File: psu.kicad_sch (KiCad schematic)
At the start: 76 parts, among them J17 Barrel_Jack_Switch, J18 USB_C_Receptacle_USB2.0_16P, Q5 2N7002, Q6 2N7002, Q7 AON7262E, U13 TL431DBZ, U15 LM2734X

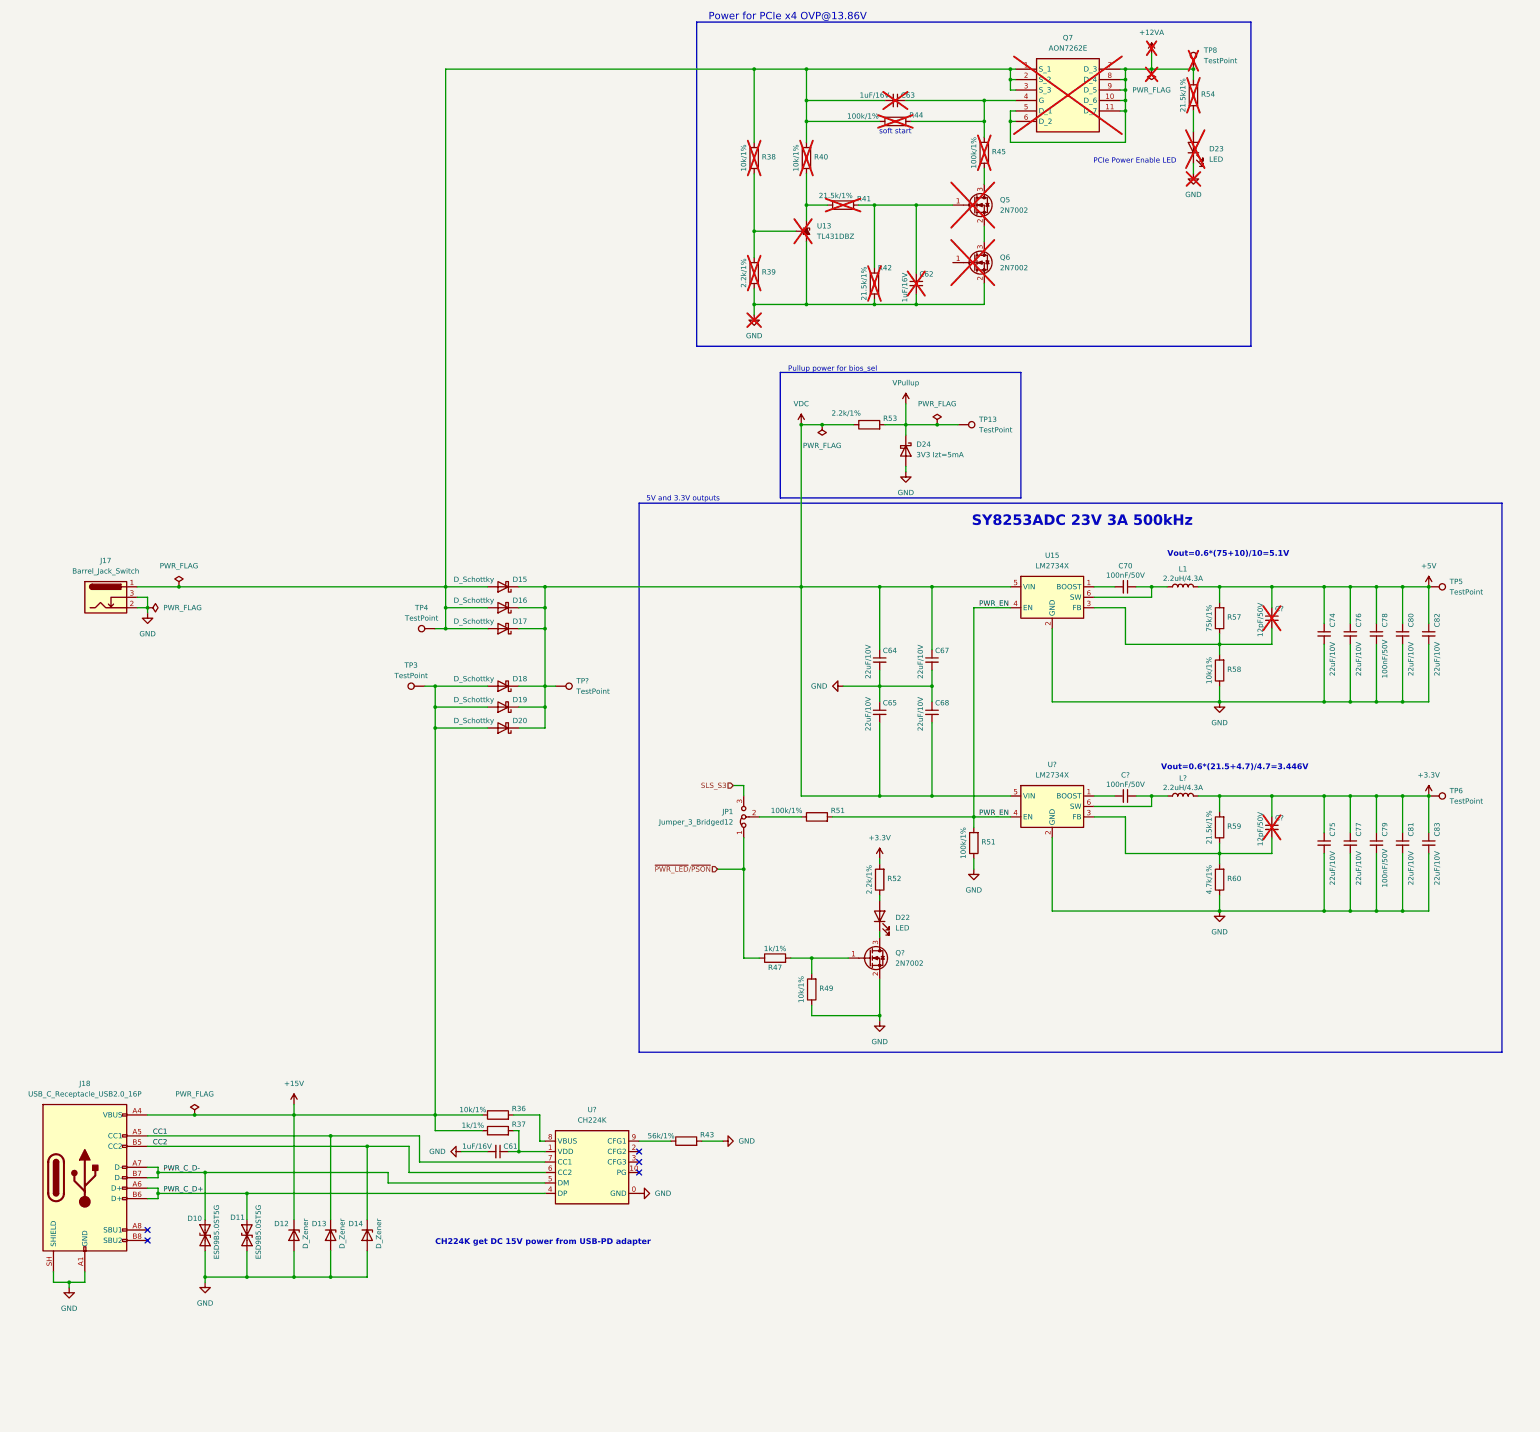
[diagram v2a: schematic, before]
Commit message: feat(psu): Added power and reset buttons
- Also added extra labels and documentation.
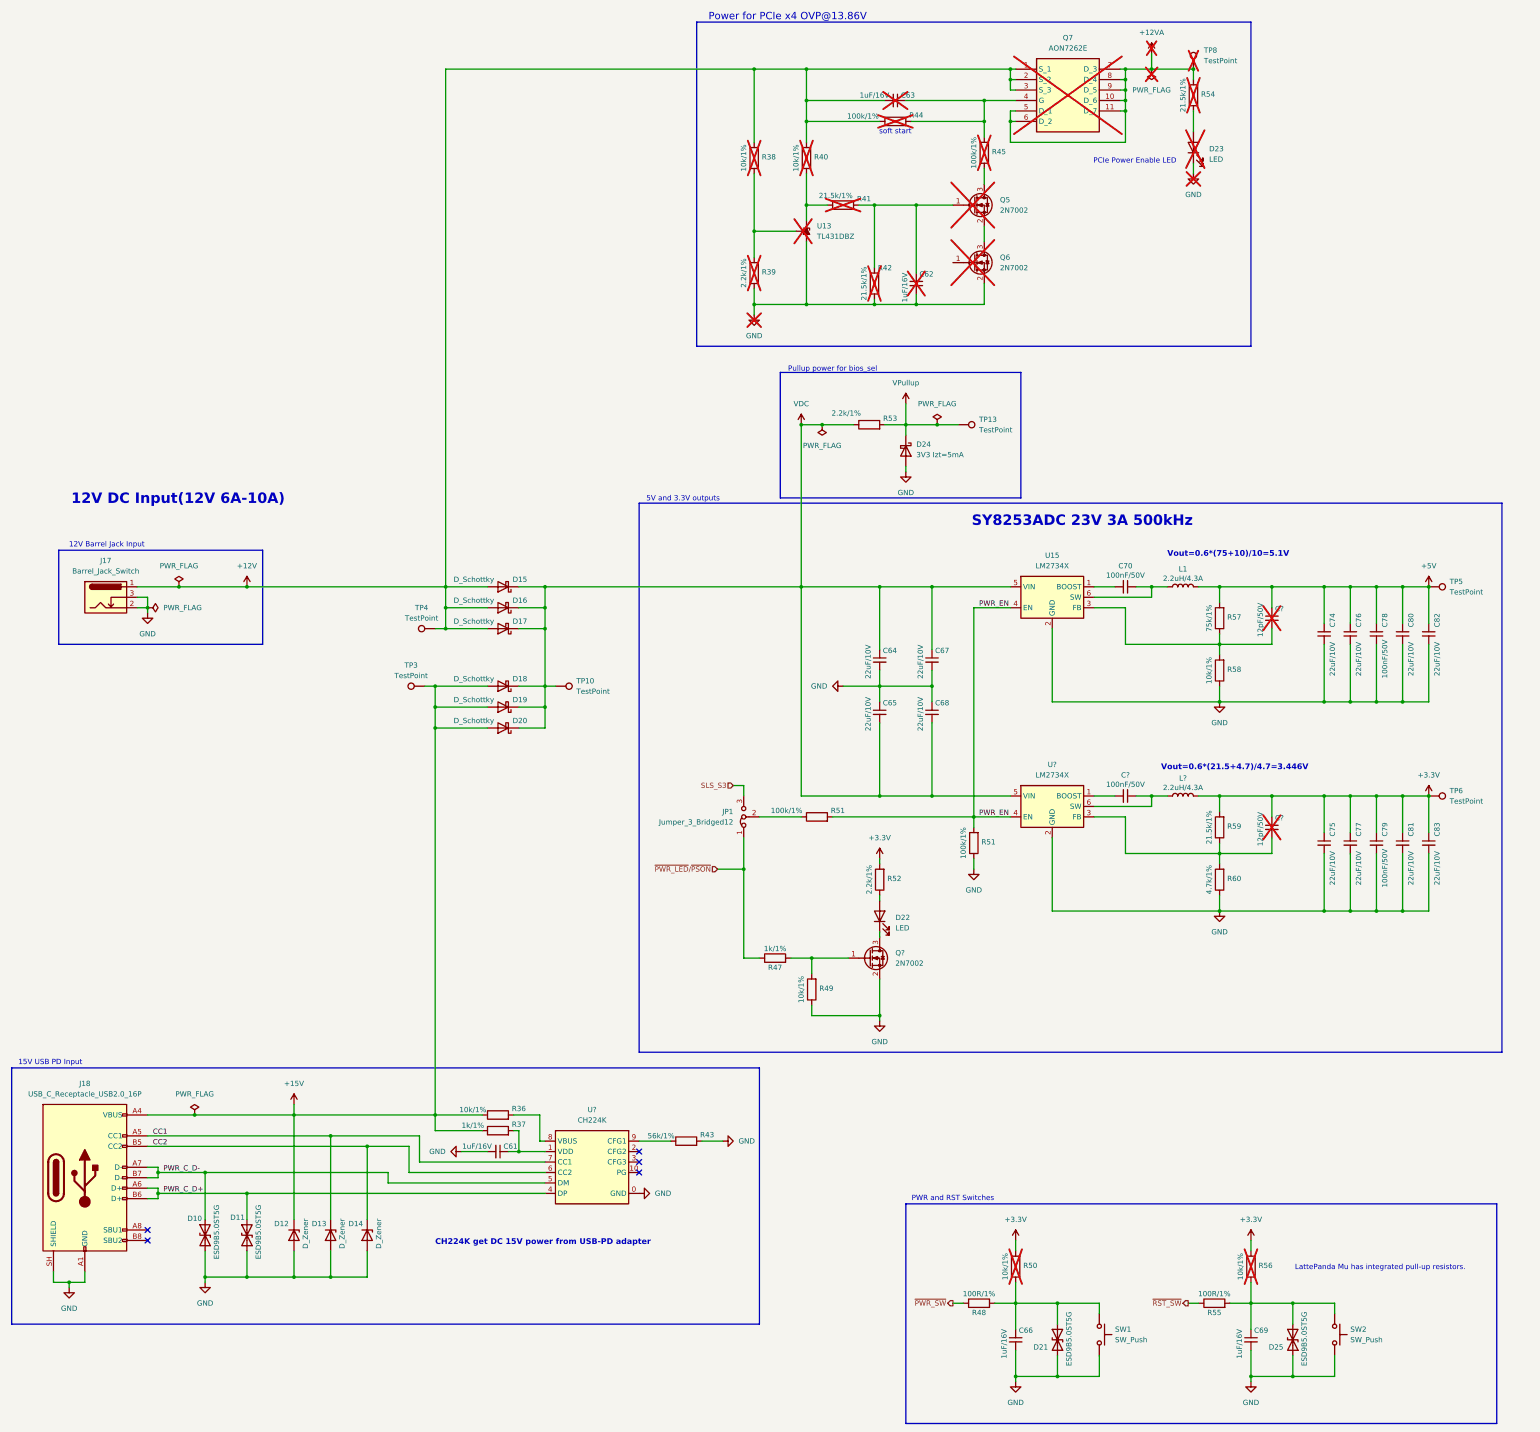
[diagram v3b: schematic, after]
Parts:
- added C66, C69: 1uF/16V, A_HDJ_Library:C_0402_1005Metric, symbol Device:C_Small
- added D21, D25: ESD9B5.0ST5G, Diode_SMD:D_0402_1005Metric, symbol Diode:ESD9B5.0ST5G
- added R48, R55: 100R/1%, A_HDJ_Library:R_0402_1005Metric, symbol Device:R
- added R50, R56: 10k/1%, A_HDJ_Library:R_0402_1005Metric, symbol Device:R
- added SW1, SW2: SW_Push, A_HDJ_Library:SW_Push_6x6x6, symbol Switch:SW_Push
- gave numbers to parts that had none: 1
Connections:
- net +3.3V: now also R50.2, R56.2
- net GND: now also C66.2, C69.2, D21.2 (A2), D25.2 (A2), SW1.2, SW2.2
- net +12V: now reaches C63.2, D15.2 (A), D16.2 (A), D17.2 (A), J17.1, Q7.1 (S_1), Q7.2 (S_2), Q7.3 (S_3), R38.2, R40.2, R44.1, TP4.1
- new net: C66.1, D21.1 (A1), R48.2, R50.1, SW1.1
- new net: C69.1, D25.1 (A1), R55.2, R56.1, SW2.1
- new net ~{PWR_SW}: R48.1
- new net ~{RST_SW}: R55.1
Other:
- note added: "12V Barrel Jack Input"
- note added: "12V DC Input(12V 6A-10A)"
- note added: "15V USB PD Input"
- note added: "LattePanda Mu has integrated pull-up resistors."
- note added: "PWR and RST Switches"

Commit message: feat: Ran ERC and fixed missing annotations and wiring errors
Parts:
- added TP9: TestPoint, symbol Connector:TestPoint
- gave numbers to parts that had none: 7
- renumbered R51 to R46
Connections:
- net PWR_EN: now also Q6.1 (G), TP9.1

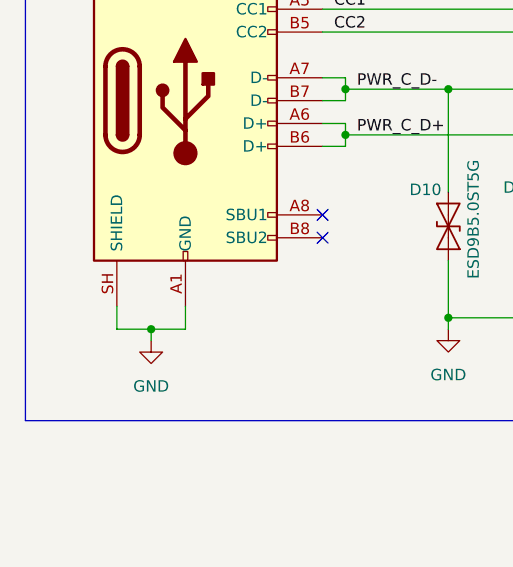
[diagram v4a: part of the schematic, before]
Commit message: fix: Set missing footprints and fixed missing pin-pad connections.
- J15, J16 missing MP1 and MP2 pins. Fixed in pin table within the symbol editor for each symbol.
- A ll USB receptacles J4, J5, J18 had mismatched pin numbers for the pcb symbol footprint. Renamed to match.
- Fixed various DNP components that were not excluded from the board.
- Fixed remaining missing footprints.
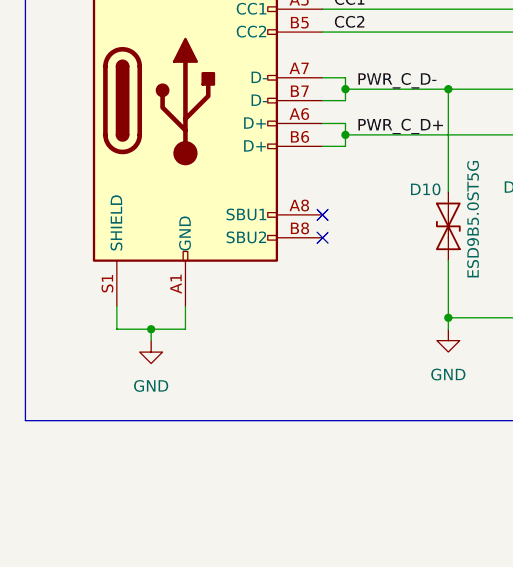
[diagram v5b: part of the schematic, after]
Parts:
- J18: footprint (none) -> A_HDJ_Library:USB_C_Receptacle_G-Switch_GT-USB-7010ASV
- JP1: footprint (none) -> A_HDJ_Library:PinHeader_1x03_P2.54mm_Vertical
- TP10, TP13, TP3, TP4, TP5, TP6, TP8, TP9: footprint (none) -> A_HDJ_Library:TestPoint_Pad_D1.5mm
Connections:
- net GND: now also J18.S1 (SHIELD); no longer J18.SH (SHIELD)

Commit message: fix: Fixed DNP parts populating on the board.
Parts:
- C62, C63, D23, Q5, Q6, Q7, R38, R39, R40, R41, R42, R44, R45, R50, R54, R56, TP8, TP9, U13: now left out of the parts list
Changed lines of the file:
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@@
 		(body_style 1)
 		(exclude_from_sim no)
-		(in_bom yes)
-		(on_board yes)
+		(in_bom no)
+		(on_board no)
 		(in_pos_files yes)
 		(dnp yes)
@@
 		(body_style 1)
 		(exclude_from_sim no)
-		(in_bom yes)
-		(on_board yes)
+		(in_bom no)
+		(on_board no)
 		(in_pos_files yes)
 		(dnp yes)
@@
 		(body_style 1)
 		(exclude_from_sim no)
-		(in_bom yes)
-		(on_board yes)
+		(in_bom no)
+		(on_board no)
 		(in_pos_files yes)
 		(dnp yes)
@@
 		(body_style 1)
 		(exclude_from_sim no)
-		(in_bom yes)
-		(on_board yes)
+		(in_bom no)
+		(on_board no)
 		(in_pos_files yes)
 		(dnp yes)
@@
 		(body_style 1)
 		(exclude_from_sim no)
-		(in_bom yes)
-		(on_board yes)
+		(in_bom no)
+		(on_board no)
 		(in_pos_files yes)
 		(dnp yes)
@@
 		(body_style 1)
 		(exclude_from_sim no)
-		(in_bom yes)
-		(on_board yes)
+		(in_bom no)
+		(on_board no)
 		(in_pos_files yes)
 		(dnp yes)
@@
 		(body_style 1)
 		(exclude_from_sim no)
-		(in_bom yes)
-		(on_board yes)
+		(in_bom no)
+		(on_board no)
 		(in_pos_files yes)
 		(dnp yes)
@@
 		(body_style 1)
 		(exclude_from_sim no)
-		(in_bom yes)
-		(on_board yes)
+		(in_bom no)
+		(on_board no)
 		(in_pos_files yes)
 		(dnp yes)
@@
 		(body_style 1)
 		(exclude_from_sim no)
-		(in_bom yes)
-		(on_board yes)
+		(in_bom no)
+		(on_board no)
 		(in_pos_files yes)
 		(dnp yes)
@@
 		(body_style 1)
 		(exclude_from_sim no)
-		(in_bom yes)
-		(on_board yes)
+		(in_bom no)
+		(on_board no)
 		(in_pos_files yes)
 		(dnp yes)
@@
 		(body_style 1)
 		(exclude_from_sim no)
-		(in_bom yes)
-		(on_board yes)
+		(in_bom no)
+		(on_board no)
 		(in_pos_files yes)
 		(dnp yes)
@@
 		(body_style 1)
 		(exclude_from_sim no)
-		(in_bom yes)
-		(on_board yes)
+		(in_bom no)
+		(on_board no)
 		(in_pos_files yes)
 		(dnp yes)
@@
 		(body_style 1)
 		(exclude_from_sim no)
-		(in_bom yes)
-		(on_board yes)
+		(in_bom no)
+		(on_board no)
 		(in_pos_files yes)
 		(dnp yes)
@@
 		(body_style 1)
 		(exclude_from_sim no)
-		(in_bom yes)
-		(on_board yes)
+		(in_bom no)
+		(on_board no)
 		(in_pos_files yes)
 		(dnp yes)
@@
 		(body_style 1)
 		(exclude_from_sim no)
-		(in_bom yes)
-		(on_board yes)
+		(in_bom no)
+		(on_board no)
 		(in_pos_files yes)
 		(dnp yes)
@@
 		(body_style 1)
 		(exclude_from_sim no)
-		(in_bom yes)
-		(on_board yes)
+		(in_bom no)
+		(on_board no)
 		(in_pos_files yes)
 		(dnp yes)
@@
 		(body_style 1)
 		(exclude_from_sim no)
-		(in_bom yes)
-		(on_board yes)
+		(in_bom no)
+		(on_board no)
 		(in_pos_files yes)
 		(dnp yes)
@@
 		(body_style 1)
 		(exclude_from_sim no)
-		(in_bom yes)
-		(on_board yes)
+		(in_bom no)
+		(on_board no)
 		(in_pos_files yes)
 		(dnp yes)
@@
 		(body_style 1)
 		(exclude_from_sim no)
-		(in_bom yes)
-		(on_board yes)
+		(in_bom no)
+		(on_board no)
 		(in_pos_files yes)
 		(dnp yes)
@@
 		(body_style 1)
 		(exclude_from_sim no)
-		(in_bom yes)
-		(on_board yes)
+		(in_bom no)
+		(on_board no)
 		(in_pos_files yes)
 		(dnp yes)
@@
 		(body_style 1)
 		(exclude_from_sim no)
-		(in_bom yes)
-		(on_board yes)
+		(in_bom no)
+		(on_board no)
 		(in_pos_files yes)
 		(dnp yes)
@@
 		(body_style 1)
 		(exclude_from_sim no)
-		(in_bom yes)
-		(on_board yes)
+		(in_bom no)
+		(on_board no)
 		(in_pos_files yes)
 		(dnp yes)
@@
 		(body_style 1)
 		(exclude_from_sim no)
-		(in_bom yes)
-		(on_board yes)
+		(in_bom no)
+		(on_board no)
 		(in_pos_files yes)
 		(dnp yes)
